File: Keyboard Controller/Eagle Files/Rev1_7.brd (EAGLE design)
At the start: 54.6 x 40.3 mm, 6 parts

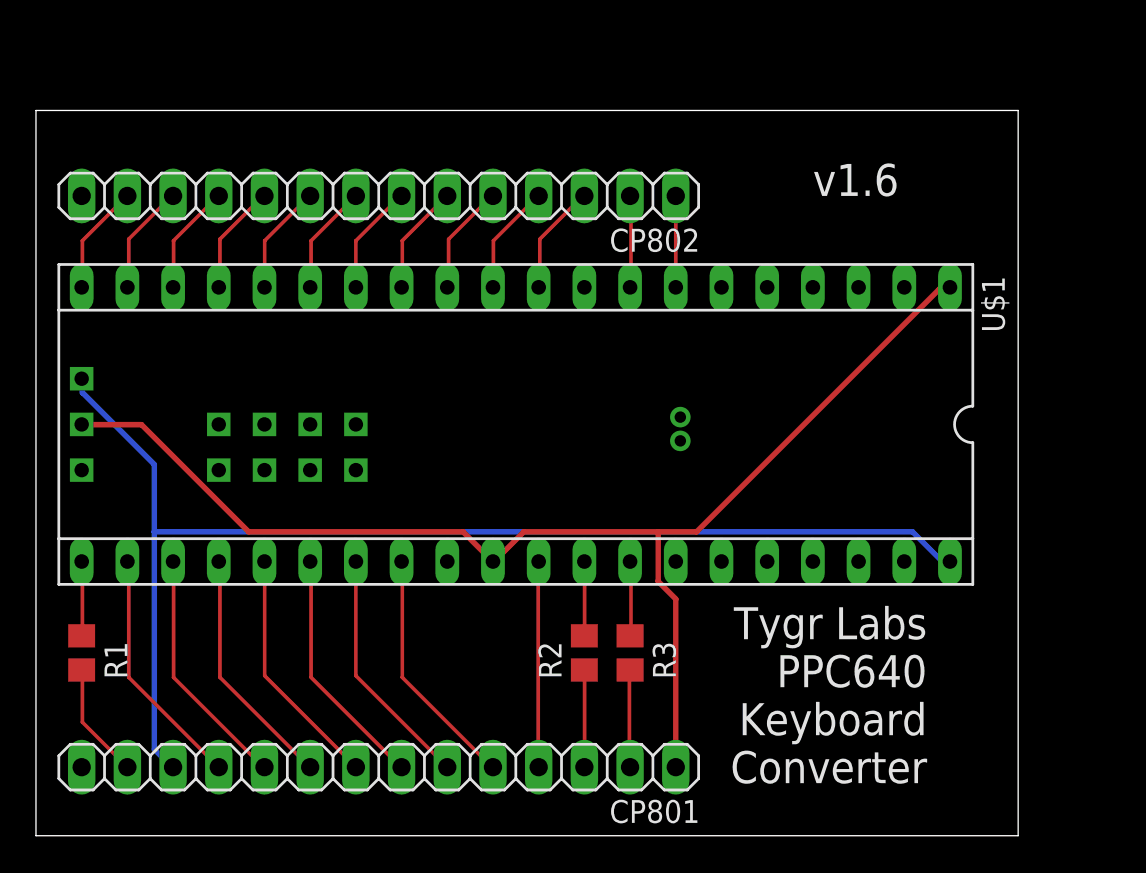
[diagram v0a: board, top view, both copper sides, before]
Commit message: Had resistor on wrong pin.
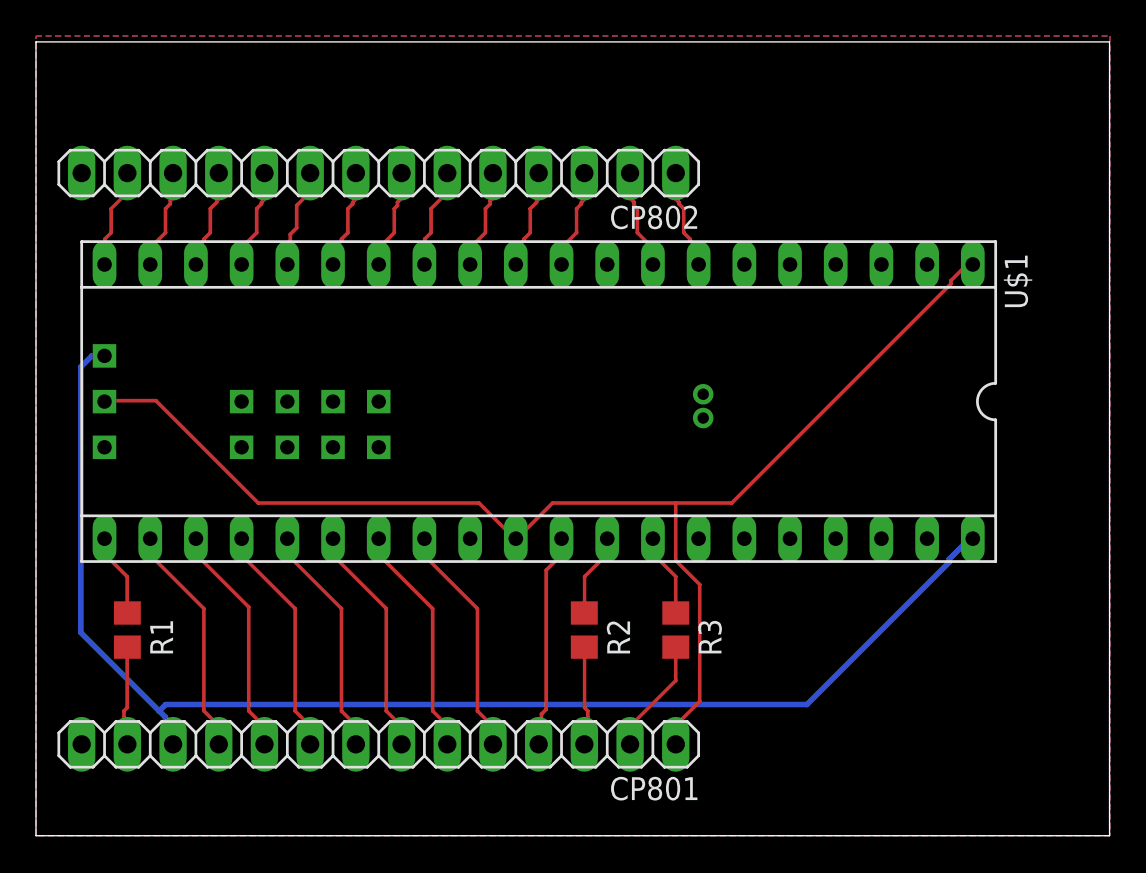
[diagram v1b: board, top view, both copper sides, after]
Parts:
- moved R1 2.84 mm to (5.08, 11.4)
- moved R3 2.84 mm to (35.6, 11.4)
- moved U$1 1.80 mm to (27.9, 24.1)
- moved CP801 1.27 mm to (19.1, 5.08)
- moved R2 1.27 mm to (30.5, 11.4)
- moved CP802 1.27 mm to (19.1, 36.8)
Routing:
- net VCC: track 68.6 -> 74.0 mm
- net GND: track 71.2 -> 72.5 mm
- net N$25: track 5.50 -> 6.45 mm
- net N$27: track 6.45 -> 5.55 mm
- net N$19: track 6.20 -> 5.61 mm
- net N$12: track 6.20 -> 5.61 mm
- net N$17: track 6.20 -> 5.62 mm
- net N$10: track 6.20 -> 5.62 mm
- net N$6: track 13.6 -> 13.0 mm
- net N$4: track 13.6 -> 13.0 mm
- net N$8: track 13.6 -> 13.0 mm
- net N$1: track 13.6 -> 13.0 mm
- net N$3: track 13.6 -> 13.0 mm
- net N$2: track 6.15 -> 5.60 mm
- net N$16: track 6.15 -> 5.60 mm
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- added copper zone on layer 1, net N$28
- added copper zone on layer 16, net N$29
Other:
- board size 54.6 x 40.3 mm -> 59.7 x 44.1 mm
- board text added: "Tygr Labs PPC640 Keyboard Converter v1.7"
- board text removed: "Tygr Labs PPC640 Keyboard Converter"
- board text removed: "v1.6"
